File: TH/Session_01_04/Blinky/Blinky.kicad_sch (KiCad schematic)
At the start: 7 parts

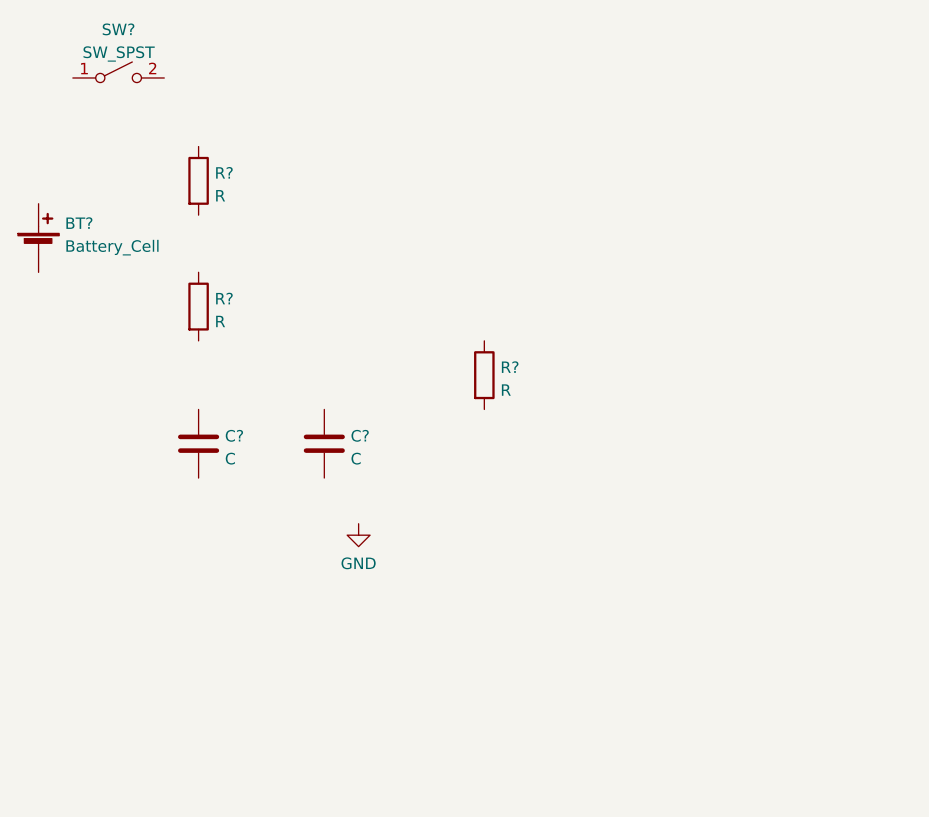
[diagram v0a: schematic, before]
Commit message: Revamps the through-hole project as transistor based
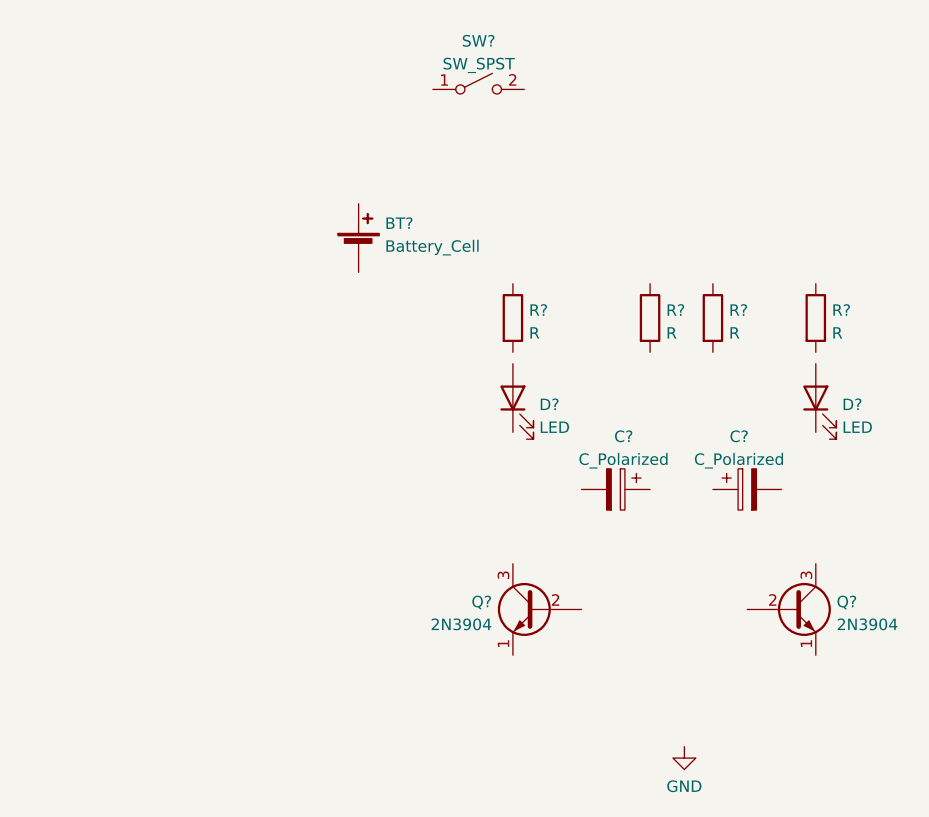
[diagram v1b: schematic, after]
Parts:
- removed C? (x2): C, symbol Device:C
- added C? (x2): C_Polarized, symbol Device:C_Polarized
- added D? (x2): LED, symbol Device:LED
- added Q? (x2): 2N3904, Package_TO_SOT_THT:TO-92_Inline, symbol Transistor_BJT:2N3904
- added R?: R, symbol Device:R
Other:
- moved on the sheet: BT?, R?, SW?
